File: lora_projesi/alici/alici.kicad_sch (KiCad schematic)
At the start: 127 parts, among them J1 USB-C, J2 SMA, J3 RJ45, J4 u.FL (ANA ANTEN), J5 12 V GIRIS, J6 LAMBA, J7 MICRO-SIM, J8 u.FL (YARDIMCI ANTEN, ISTEGE 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, K1 SRD-12VDC-SL-A, Q1 AO3401A, Q2 MMBT2222A, Q3 MMBT2222A, Q4 MMBT2222A, SW1 DUGME, U1 ESP32-S3-WROOM-1-N4, U10 SIM7600SA, U11 AP2112K-3.3, U12 ESDA6V1-5SC6, U4 RFM95W-915S2, U5 TPS62933DRLR, U6 TPS62933DRLR, U7 USBLC6-2SC6, U8 TXB0104PW, U9 W5500, Y1 25 MHz

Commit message: Alici: 0 baglantisiz, 0 DRC hatasi; sema/xml TXB0104 A4/B4 toprak duzeltmesi
Co-Authored-By: Claude Sonnet 5.5 <noreply@anthropic.com>
Claude-Session: https://claude.ai/code/session_01Q71gHQtKJ86ZE2CtYTYSwP
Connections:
- net GND: now also U8.10 (B4), U8.5 (A4)
- no-connect marks 93 -> 91

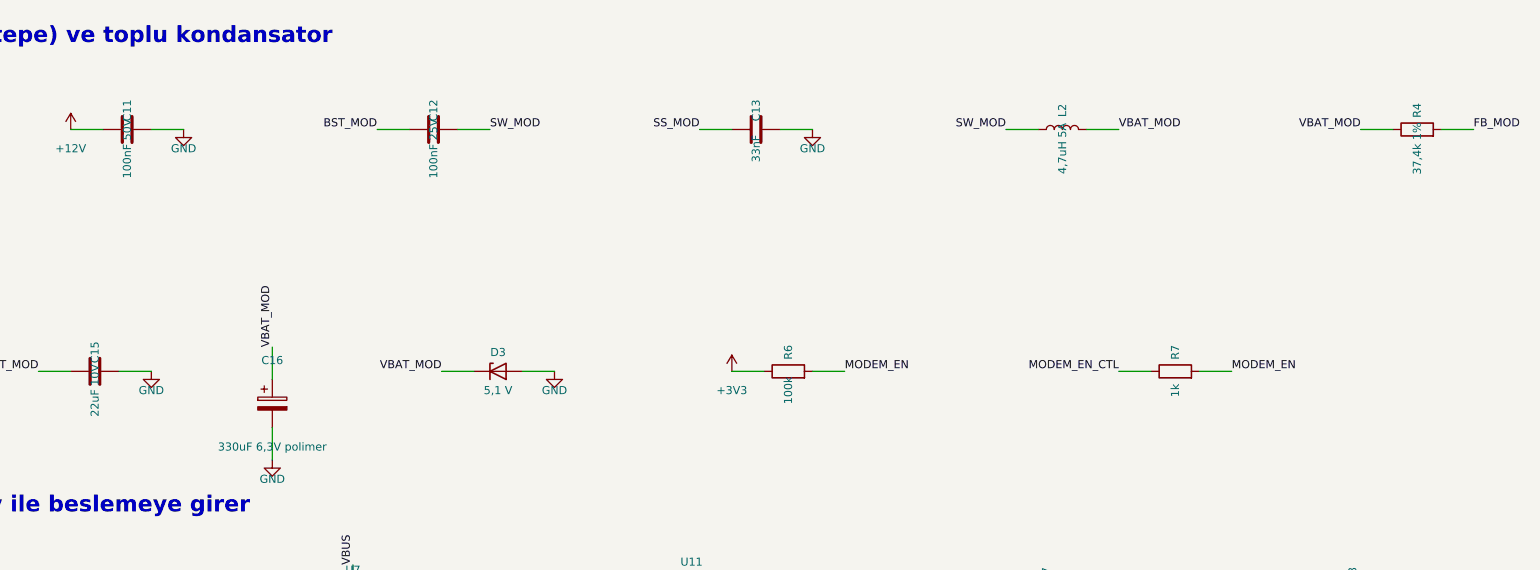
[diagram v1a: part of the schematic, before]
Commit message: VBAT 4,0 V + polimer ESR sarti; gercekci simulasyonlar ve maliyet modeli
Co-Authored-By: Claude Sonnet 5.5 <noreply@anthropic.com>
Claude-Session: https://claude.ai/code/session_01Q71gHQtKJ86ZE2CtYTYSwP
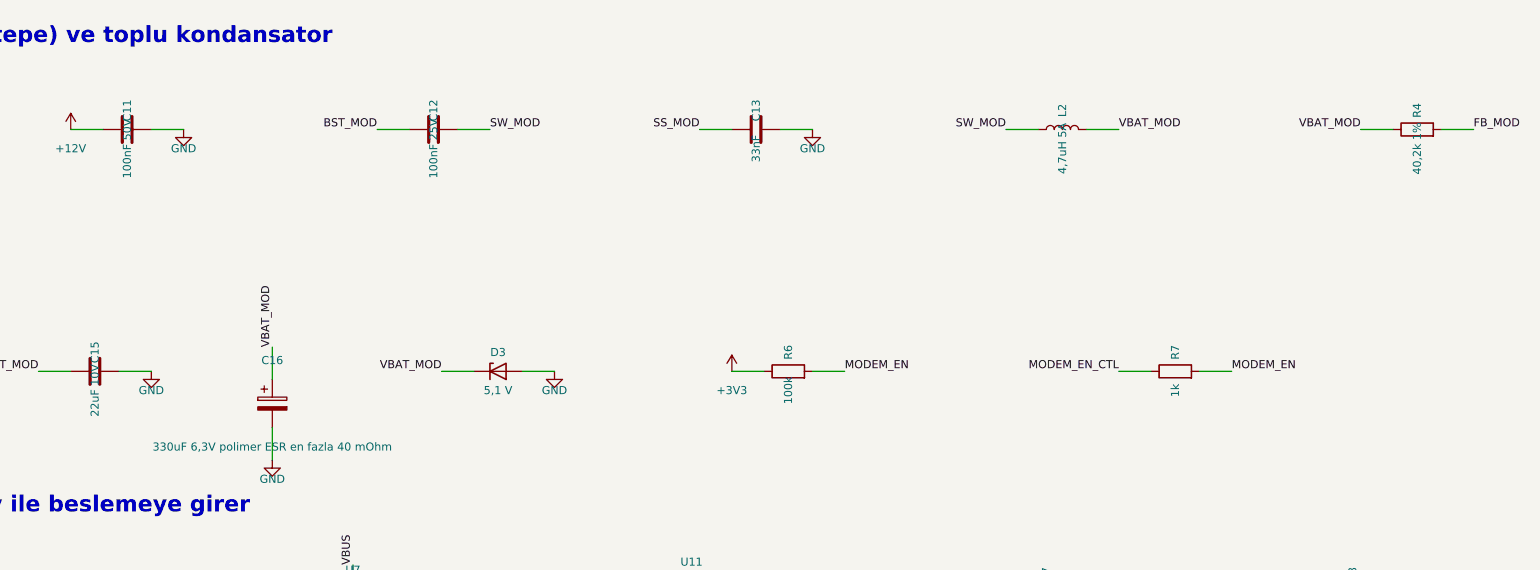
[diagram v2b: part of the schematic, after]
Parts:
- C16: value 330uF 6,3V polimer -> 330uF 6,3V polimer ESR en fazla 40 mOhm
- R4: value 37,4k 1% -> 40,2k 1%
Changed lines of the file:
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@@
     (in_bom yes) (on_board yes) (dnp no)
     (property "Reference" "R4" (at 345.44 136.7 0) (effects (font (size 1.27 1.27))))
-    (property "Value" "37,4k 1%" (at 345.44 142.7 0) (effects (font (size 1.27 1.27))))
+    (property "Value" "40,2k 1%" (at 345.44 142.7 0) (effects (font (size 1.27 1.27))))
     (property "Footprint" "Resistor_SMD:R_0603_1608Metric" (at 345.44 139.7 0) (effects (font (size 1.27 1.27)) hide))
     (property "Datasheet" "" (at 345.44 139.7 0) (effects (font (size 1.27 1.27)) hide))
@@
     (in_bom yes) (on_board yes) (dnp no)
     (property "Reference" "C16" (at 165.1 176.07 0) (effects (font (size 1.27 1.27))))
-    (property "Value" "330uF 6,3V polimer" (at 165.1 189.69 0) (effects (font (size 1.27 1.27))))
+    (property "Value" "330uF 6,3V polimer ESR en fazla 40 mOhm" (at 165.1 189.69 0) (effects (font (size 1.27 1.27))))
     (property "Footprint" "Capacitor_SMD:CP_Elec_6.3x7.7" (at 165.1 182.88 0) (effects (font (size 1.27 1.27)) hide))
     (property "Datasheet" "" (at 165.1 182.88 0) (effects (font (size 1.27 1.27)) hide))

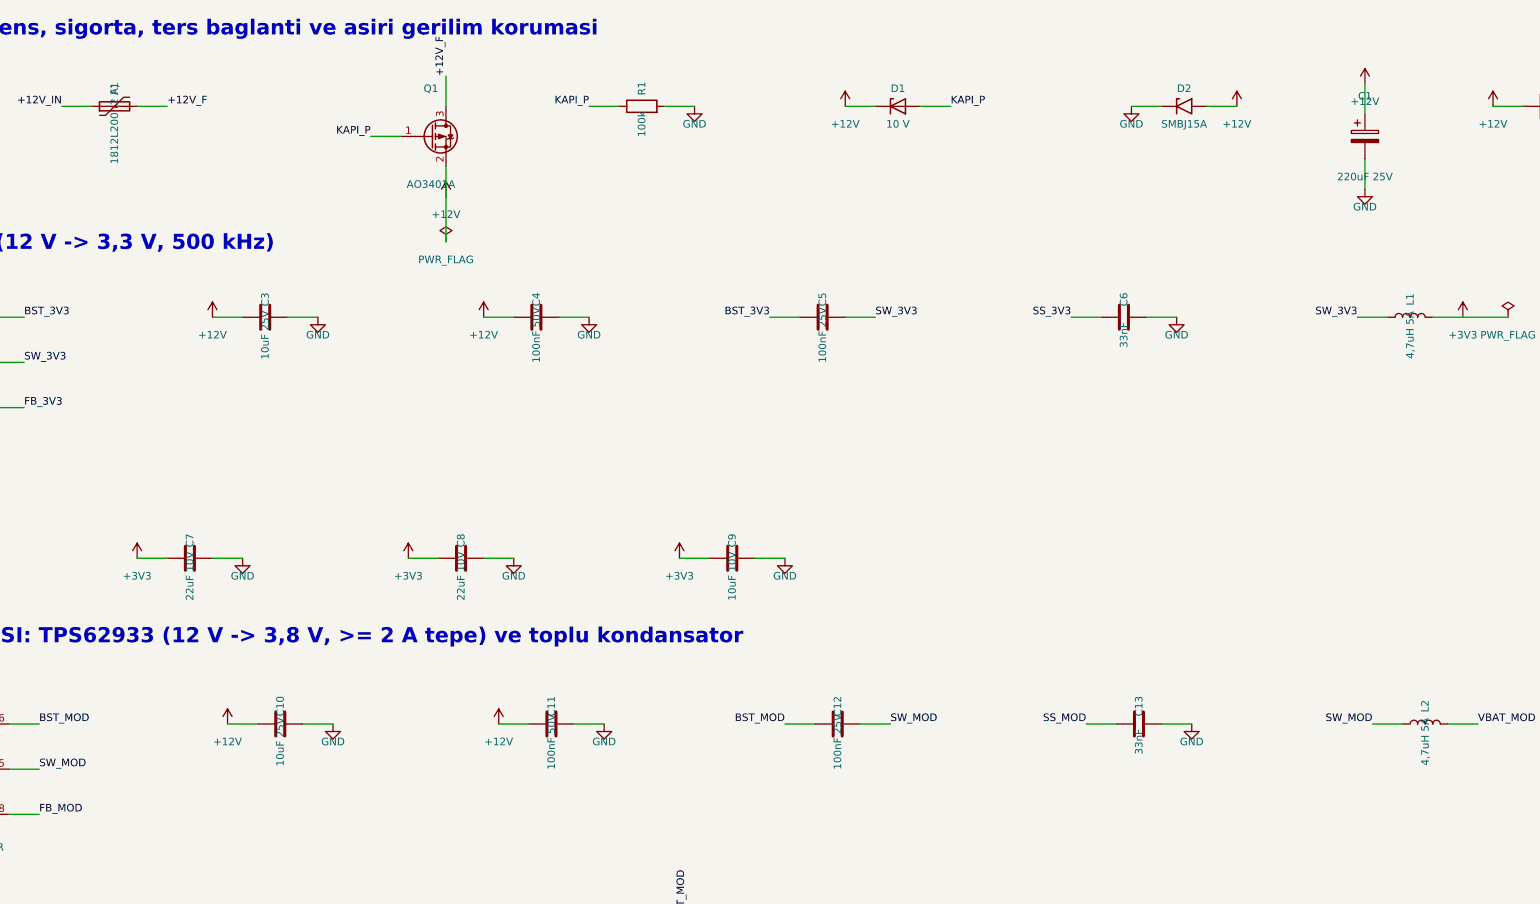
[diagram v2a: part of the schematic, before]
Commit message: Parca belgeleri okundu: PTC son eki, endüktör Isat, BST dielektrik, kristal sarti; BELGELER.md
Co-Authored-By: Claude Sonnet 5.5 <noreply@anthropic.com>
Claude-Session: https://claude.ai/code/session_01Q71gHQtKJ86ZE2CtYTYSwP
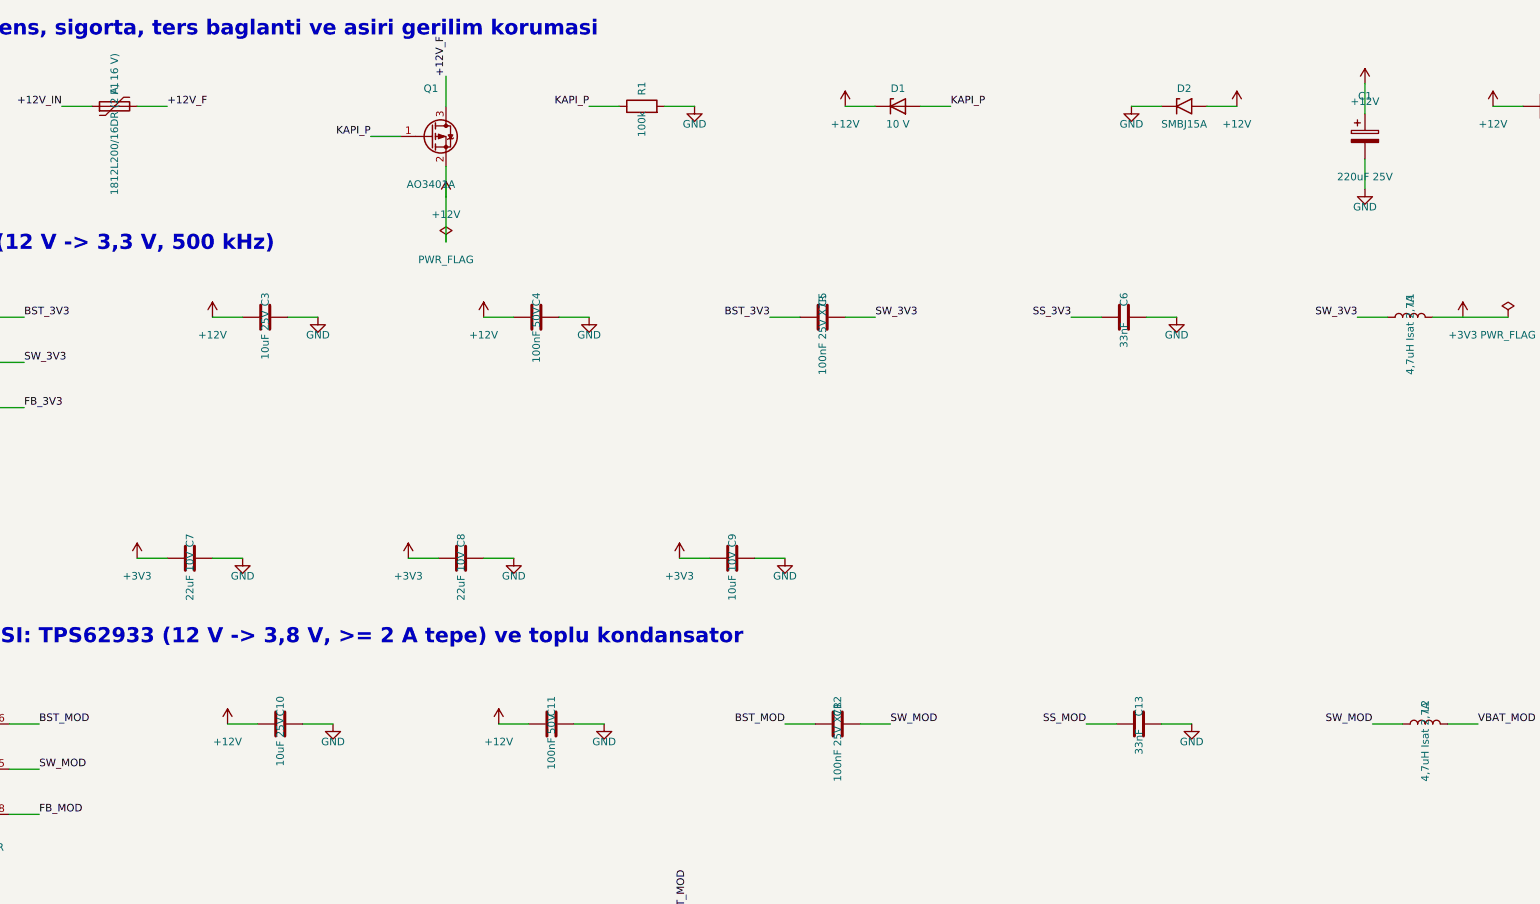
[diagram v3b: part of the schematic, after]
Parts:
- C12, C5: value 100nF 25V -> 100nF 25V X7R
- F1: value 1812L200 (2 A) -> 1812L200/16DR (2 A, 16 V); MPN PTC 2 A tutma, 1812 -> Littelfuse 1812L200/16DR (tutma 2 A, 16 V; 8 V olan 1812L20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
- K1: MPN Songle SRD-12VDC-SL-A -> Songle SRD-12VDC-SL-A (bobin 400 ohm, kontak 10 A 30 VDC)
- L1, L2: value 4,7uH 5A -> 4,7uH Isat 2,7A; MPN 4,7uH, Isat >= 5 A (Bourns SRN6028 sinifi) -> Bourns SRN6028-4R7M (Isat 2,7 A, Irms 3 A, DCR 38 mOhm; dag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
- Y1: MPN 25 MHz, 18 pF yuk -> 25 MHz, 18 pF yuk, +-30 ppm, C0 en fazla 7 pF (W5500 belges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
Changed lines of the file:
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@@
     (in_bom yes) (on_board yes) (dnp no)
     (property "Reference" "F1" (at 68.58 32.56 0) (effects (font (size 1.27 1.27))))
-    (property "Value" "1812L200 (2 A)" (at 68.58 38.56 0) (effects (font (size 1.27 1.27))))
+    (property "Value" "1812L200/16DR (2 A, 16 V)" (at 68.58 38.56 0) (effects (font (size 1.27 1.27))))
     (property "Footprint" "Fuse:Fuse_1812_4532Metric" (at 68.58 35.56 0) (effects (font (size 1.27 1.27)) hide))
     (property "Datasheet" "" (at 68.58 35.56 0) (effects (font (size 1.27 1.27)) hide))
-    (property "MPN" "PTC 2 A tutma, 1812" (at 68.58 35.56 0) (effects (font (size 1.27 1.27)) hide))
+    (property "MPN" "Littelfuse 1812L200/16DR (tutma 2 A, 16 V; 8 V olan 1812L200TH kullanilmaz)" (at 68.58 35.56 0) (effects (font (size 1.27 1.27)) hide))
     (pin "1")
     (pin "2")
@@
     (in_bom yes) (on_board yes) (dnp no)
     (property "Reference" "C5" (at 187.96 68.12 0) (effects (font (size 1.27 1.27))))
-    (property "Value" "100nF 25V" (at 187.96 74.12 0) (effects (font (size 1.27 1.27))))
+    (property "Value" "100nF 25V X7R" (at 187.96 74.12 0) (effects (font (size 1.27 1.27))))
     (property "Footprint" "Capacitor_SMD:C_0603_1608Metric" (at 187.96 71.12 0) (effects (font (size 1.27 1.27)) hide))
     (property "Datasheet" "" (at 187.96 71.12 0) (effects (font (size 1.27 1.27)) hide))
@@
     (in_bom yes) (on_board yes) (dnp no)
     (property "Reference" "L1" (at 287.02 68.12 0) (effects (font (size 1.27 1.27))))
-    (property "Value" "4,7uH 5A" (at 287.02 74.12 0) (effects (font (size 1.27 1.27))))
+    (property "Value" "4,7uH Isat 2,7A" (at 287.02 74.12 0) (effects (font (size 1.27 1.27))))
     (property "Footprint" "Inductor_SMD:L_Bourns-SRN6028" (at 287.02 71.12 0) (effects (font (size 1.27 1.27)) hide))
     (property "Datasheet" "" (at 287.02 71.12 0) (effects (font (size 1.27 1.27)) hide))
-    (property "MPN" "4,7uH, Isat >= 5 A (Bourns SRN6028 sinifi)" (at 287.02 71.12 0) (effects (font (size 1.27 1.27)) hide))
+    (property "MPN" "Bourns SRN6028-4R7M (Isat 2,7 A, Irms 3 A, DCR 38 mOhm; dagitimci listesi)" (at 287.02 71.12 0) (effects (font (size 1.27 1.27)) hide))
     (pin "1")
     (pin "2")
@@
     (in_bom yes) (on_board yes) (dnp no)
     (property "Reference" "C12" (at 190.5 136.7 0) (effects (font (size 1.27 1.27))))
-    (property "Value" "100nF 25V" (at 190.5 142.7 0) (effects (font (size 1.27 1.27))))
+    (property "Value" "100nF 25V X7R" (at 190.5 142.7 0) (effects (font (size 1.27 1.27))))
     (property "Footprint" "Capacitor_SMD:C_0603_1608Metric" (at 190.5 139.7 0) (effects (font (size 1.27 1.27)) hide))
     (property "Datasheet" "" (at 190.5 139.7 0) (effects (font (size 1.27 1.27)) hide))
@@
     (in_bom yes) (on_board yes) (dnp no)
     (property "Reference" "L2" (at 289.56 136.7 0) (effects (font (size 1.27 1.27))))
-    (property "Value" "4,7uH 5A" (at 289.56 142.7 0) (effects (font (size 1.27 1.27))))
+    (property "Value" "4,7uH Isat 2,7A" (at 289.56 142.7 0) (effects (font (size 1.27 1.27))))
     (property "Footprint" "Inductor_SMD:L_Bourns-SRN6028" (at 289.56 139.7 0) (effects (font (size 1.27 1.27)) hide))
     (property "Datasheet" "" (at 289.56 139.7 0) (effects (font (size 1.27 1.27)) hide))
-    (property "MPN" "4,7uH, Isat >= 5 A (Bourns SRN6028 sinifi)" (at 289.56 139.7 0) (effects (font (size 1.27 1.27)) hide))
+    (property "MPN" "Bourns SRN6028-4R7M (Isat 2,7 A, Irms 3 A, DCR 38 mOhm; dagitimci listesi)" (at 289.56 139.7 0) (effects (font (size 1.27 1.27)) hide))
     (pin "1")
     (pin "2")
@@
     (property "Footprint" "Crystal:Crystal_SMD_3225-4Pin_3.2x2.5mm" (at 78.74 599.44 0) (effects (font (size 1.27 1.27)) hide))
     (property "Datasheet" "" (at 78.74 599.44 0) (effects (font (size 1.27 1.27)) hide))
-    (property "MPN" "25 MHz, 18 pF yuk" (at 78.74 599.44 0) (effects (font (size 1.27 1.27)) hide))
+    (property "MPN" "25 MHz, 18 pF yuk, +-30 ppm, C0 en fazla 7 pF (W5500 belgesi 5.5.3)" (at 78.74 599.44 0) (effects (font (size 1.27 1.27)) hide))
     (pin "1")
     (pin "2")
@@
     (property "Footprint" "Relay_THT:Relay_SPST_SANYOU_SRD_Series_Form_A" (at 22.86 868.68 0) (effects (font (size 1.27 1.27)) hide))
     (property "Datasheet" "" (at 22.86 868.68 0) (effects (font (size 1.27 1.27)) hide))
-    (property "MPN" "Songle SRD-12VDC-SL-A" (at 22.86 868.68 0) (effects (font (size 1.27 1.27)) hide))
-    (pin "1")
-    (pin "2")
+    (property "MPN" "Songle SRD-12VDC-SL-A (bobin 400 ohm, kontak 10 A 30 VDC)" (at 22.86 868.68 0) (effects (font (size 1.27 1.27)) hide))
+    (pin "1")
+    (pin "2")

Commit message: A7670SA, Ra-01H, LM66100 ideal diyot, SRP7028A, USBLC6-2: uretec ve kutuphane (kart yonlendirmesi suruyor)
Co-Authored-By: Claude Sonnet 5.5 <noreply@anthropic.com>
Claude-Session: https://claude.ai/code/session_01Q71gHQtKJ86ZE2CtYTYSwP
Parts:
- removed D4: SS14, Diode_SMD:D_SMA, symbol Diode:SS14
- removed J8: u.FL (YARDIMCI ANTEN, ISTEGE BAGLI), Connector_Coaxial:U.FL_Hirose_U.FL-R-SMT-1_Vertical, symbol Connector:Conn_Coaxial
- removed R36: 0, Resistor_SMD:R_0603_1608Metric, symbol Device:R
- removed U10: SIM7600SA, Simcom:SIM7600_LCC87, symbol Simcom:SIM7600SA
- removed U12: ESDA6V1-5SC6, Package_TO_SOT_SMD:SOT-23-6, symbol Power_Protection:ESDA6V1-5SC6
- removed U4: RFM95W-915S2, RF_Module:HOPERF_RFM9XW_SMD, symbol RF_Module:RFM95W-915S2
- added C52: 33pF, Capacitor_SMD:C_0603_1608Metric, symbol Device:C
- added C53: 10pF, Capacitor_SMD:C_0603_1608Metric, symbol Device:C
- added C54: 1uF, Capacitor_SMD:C_0603_1608Metric, symbol Device:C
- added R39, R40, R41: 22, Resistor_SMD:R_0603_1608Metric, symbol Device:R
- added TP4: USB_VBUS, TestPoint:TestPoint_Pad_1.0x1.0mm, symbol Connector:TestPoint
- added TP5: UART_LOG_TX, TestPoint:TestPoint_Pad_1.0x1.0mm, symbol Connector:TestPoint
- added U10: A7670SA, Simcom:A7670SA_LGA88, symbol Simcom:A7670SA
- added U12, U13, U14: USBLC6-2SC6, Package_TO_SOT_SMD:SOT-23-6, symbol Power_Protection:USBLC6-2SC6
- added U15: LM66100, Package_TO_SOT_SMD:SOT-363_SC-70-6, symbol Ozel:LM66100
- added U4: Ra-01H, Ozel:Ra-01H, symbol Ozel:Ra-01H
- C44, C45: value 100nF -> 1nF; MPN (none) -> A7670 belgesi: PWRKEY ve RESET uzerinde 10 nF ustu kondansa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
- L1, L2: value 4,7uH Isat 2,7A -> 4,7uH Isat 10A; footprint Inductor_SMD:L_Bourns-SRN6028 -> Inductor_SMD:L_Bourns_SRP7028A_7.3x6.6mm; MPN Bourns SRN6028-4R7M (Isat 2,7 A, Irms 3 A, DCR 38 mOhm; dag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 -> Bourns SRP7028A-4R7M (Isat 10 A, Irms 5,5 A, DCR 40 mOhm; L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
- TP1: value BOOT_CFG0 -> USB_BOOT
- TP2: value USB_DN -> USB_DM
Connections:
- net +1V8: now also U10.15 (VDD_1V8)
- net +3V3: now also U15.3 (CE), U15.6 (VOUT), U4.3 (VDD)
- net +3V3_USB: now also U15.1 (VIN)
- net ANT_RF: now also U4.1 (ANT)
- net GND: now also C52.2, C53.2, C54.2, U10.17 (GND), U10.18 (GND), U10.2 (GND), U10.29 (GND), U10.39 (GND), U10.45 (GND), U10.46 (GND), U10.54 (GND), U10.58 (GND), U10.59 (GND), U10.61 (GND), U10.62 (GND), U10.63 (GND), U10.64 (GND), U10.65 (GND), U10.69 (GND), U10.70 (GND), U10.71 (GND), U10.72 (GND), U10.73 (GND), U10.74 (GND), U10.75 (GND), U10.76 (GND), U10.77 (GND), U10.78 (GND), U10.79 (GND), U10.80 (GND), U10.81 (GND), U10.82 (GND), U10.83 (GND), U10.84 (GND), U10.85 (GND), U10.86 (GND), U10.87 (GND), U10.88 (GND), U12.2 (GND), U13.2 (GND), U14.2 (GND), U15.2 (GND), U15.5 (ST), U4.16 (GND), U4.2 (GND), U4.9 (GND)
- net LORA_DIO0: now also U4.5 (DIO0)
- net LORA_DIO1: now also U4.6 (DIO1)
- net LORA_NSS: now also U4.15 (NSS)
- net LORA_RESET: now also U4.4 (RESET)
- net MODEM_ANT: now also U10.60 (RF_ANT)
- net MODEM_RESET: now also U10.16 (RESET), U13.3 (I/O2), U13.4 (I/O2)
- net M_RXD: now also U10.10 (RXD)
- net M_STATUS: now also U10.66 (STATUS)
- net M_TXD: now also U10.9 (TXD)
- net M_USB_DN: now also U10.28 (USB_DM)
- net M_USB_DP: now also U10.27 (USB_DP)
- net PWRKEY: now also U10.1 (PWRKEY), U13.1 (I/O1), U13.6 (I/O1)
- net SPI_MISO: now also U4.13 (MISO)
- net SPI_MOSI: now also U4.14 (MOSI)
- net SPI_SCK: now also U4.12 (SCK)
- net USIM_CLK: now also R40.2, U12.3 (I/O2), U12.4 (I/O2)
- net USIM_DATA: now also R41.2, U14.1 (I/O1), U14.6 (I/O1)
- net USIM_RST: now also R39.2, U12.1 (I/O1), U12.6 (I/O1)
- net USIM_VDD: now also U10.30 (SIM_VDD), U12.5 (VBUS), U14.5 (VBUS)
- net VBAT_MOD: now also C52.1, C53.1, C54.1, U10.55 (VBAT), U10.56 (VBAT), U10.57 (VBAT), U13.5 (VBUS)
- net BOOT_CFG0 renamed USB_BOOT
- net USB_BOOT: now also U10.6 (USB_BOOT)
- new net LOG_TX: TP5.1, U10.23 (UART_LOG_TX)
- new net M_USB_VBUS: TP4.1, U10.24 (VBUS)
- new net USIM_CLK_M: R40.1, U10.32 (SIM_CLK)
- new net USIM_DATA_M: R41.1, U10.31 (SIM_DATA)
- new net USIM_RST_M: R39.1, U10.33 (SIM_RST)
- no-connect marks 91 -> 78
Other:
- note added: "4G MODEM: A7670SA (SIMCom), SIM yuvasi, anten, seviye cevirici"
- note added: "LoRa: Ra-01H (SX1276, 803-930 MHz)"
- note added: "MODEM BESLEMESI: TPS62933 (12 V -> 4,0 V, >= 2 A tepe) ve toplu kondansator"
- note added: "USB-C: programlama; 5 V yalniz 3,3 V LDO ve ideal diyot (LM66100) ile beslemeye girer"
- note removed: "4G MODEM: SIM7600SA (SIMCom), SIM yuvasi, anten, seviye cevirici"
- note removed: "LoRa: RFM95W-915S2"
- note removed: "MODEM BESLEMESI: TPS62933 (12 V -> 3,8 V, >= 2 A tepe) ve toplu kondansator"
- note removed: "USB-C: programlama; 5 V yalniz 3,3 V LDO ve Schottky ile beslemeye girer"
